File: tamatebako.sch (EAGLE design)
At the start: 16 parts, among them CON1 PH_CONNECTOR_2PIN, CON2 PH_CONNECTOR_2PIN, SW1 IS-2235, SW3 PUSHSW, U1 ARDUINO-PRO-MINI-3.3, U2 RN42, U3 XCL101-MODULE-C331BR-G, U4 UART_MODULE

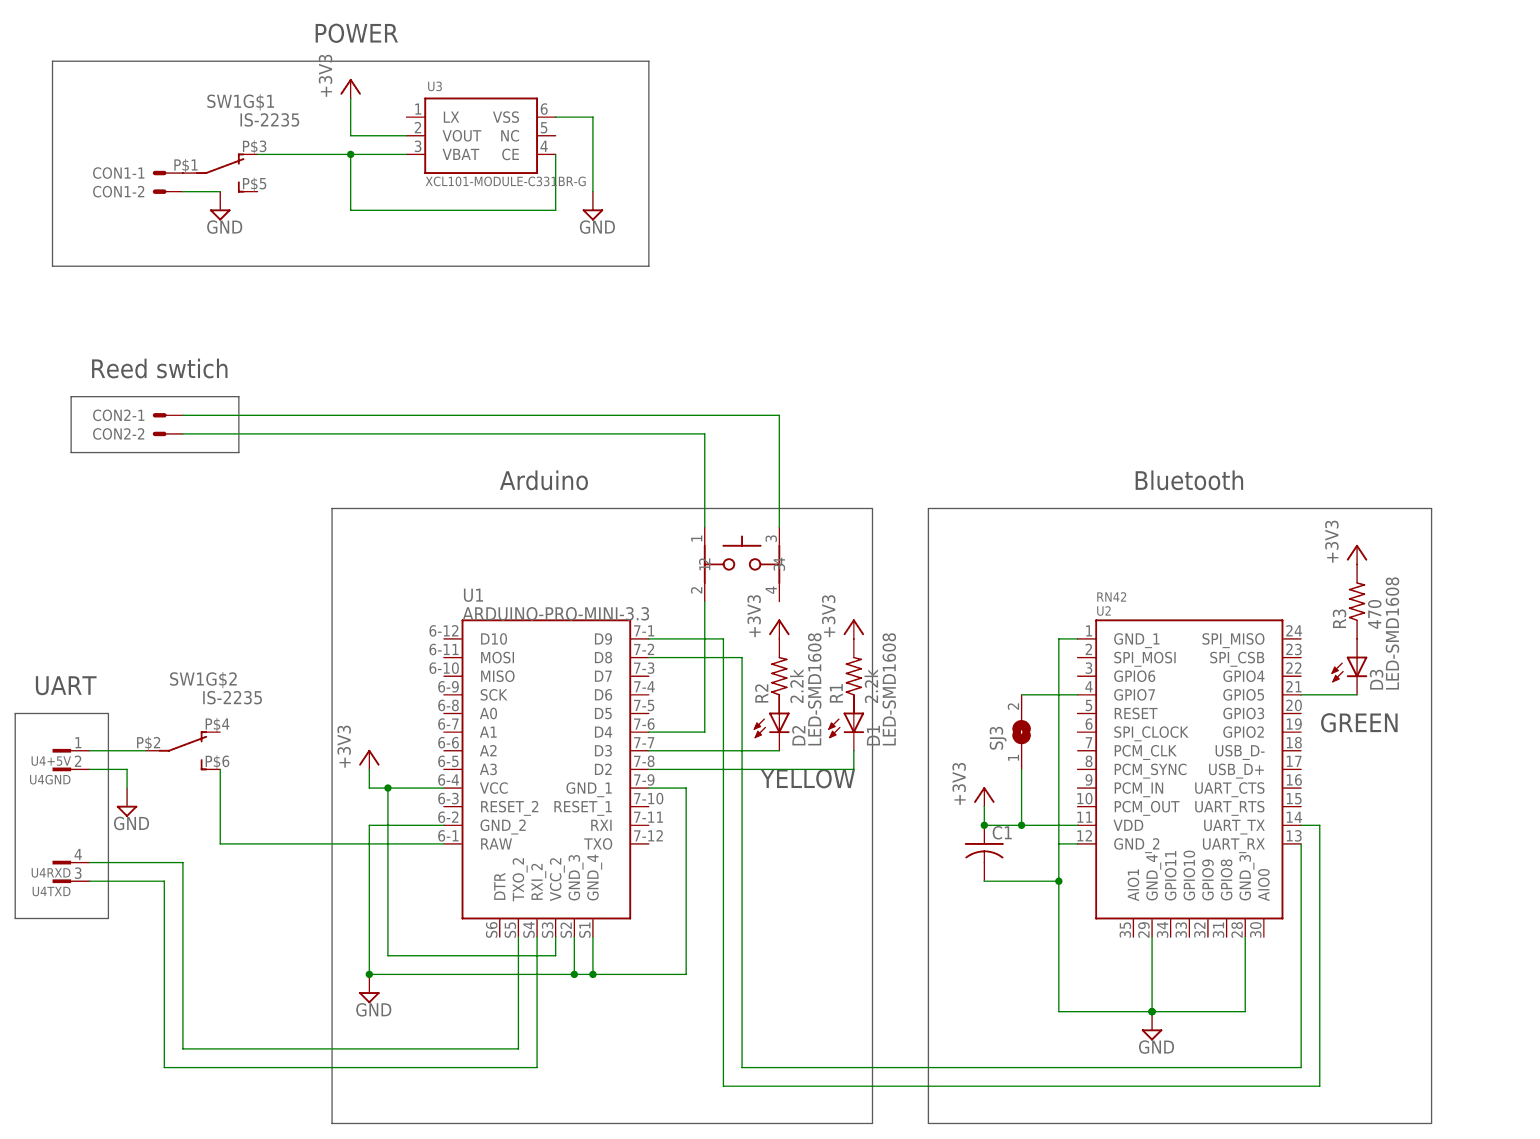
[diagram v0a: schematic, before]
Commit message: ロータリースイッチの追加とボード図の作成
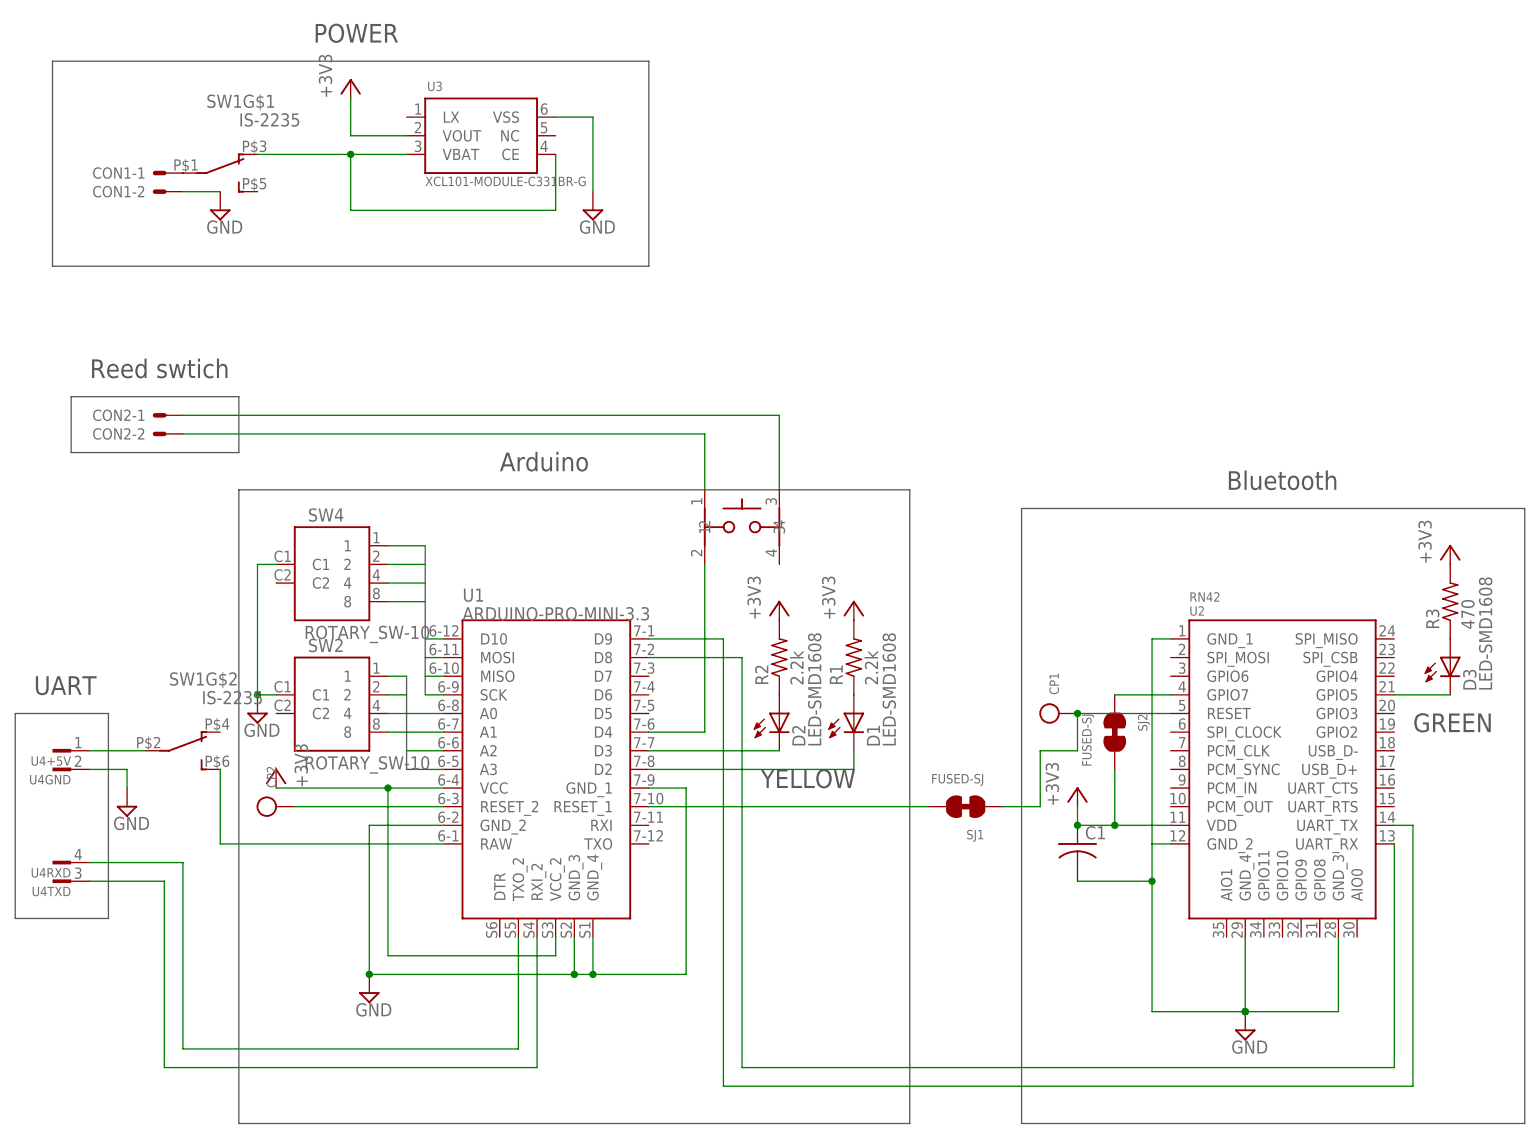
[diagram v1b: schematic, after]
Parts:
- removed SJ3: (no value), Connector_Robotech:SJ
- added CP1, CP2: SST-1-2, Connector_Robotech:SST-1-2
- added SJ1, SJ2: FUSED-SJ, mylibrary:FUSED-SJ
- added SW2, SW4: ROTARY_SW-10, mylibrary:ROTARY_SW-10
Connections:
- new net LOWER0: SW2.1, U1.A0
- new net LOWER1: SW2.2, U1.A1
- new net LOWER2: SW2.4, U1.A2
- new net LOWER3: SW2.8, U1.A3
- new net N$3: CP1.SIGNAL, SJ1.P$1, U2.RESET
- new net N$6: D1.A, R1.1
- new net N$7: D2.A, R2.1
- new net RESET_ARDUINO: SJ1.P$2, U1.RESET_1
- new net RESET_ARDUINO_2: CP2.SIGNAL, U1.RESET_2
- new net UPPER0: SW4.1, U1.D10
- new net UPPER1: SW4.2, U1.MOSI
- new net UPPER2: SW4.4, U1.MISO
- new net UPPER3: SW4.8, U1.SCK
- net +3V3: now also SJ2.P$2; no longer SJ3.1
- net GND: now also SW2.C1, SW4.C1
- net N$16: now also SJ2.P$1; no longer SJ3.2
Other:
- moved on the sheet: C1, D3, R1, R2, R3, U2
